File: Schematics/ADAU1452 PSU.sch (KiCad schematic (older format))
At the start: 74 parts, among them P301 CONN_2x1, P302 CONN_2x1, P303 PIN, P304 PIN, P305 PIN, P306 PIN, U301 IC-REG-XRP7659ISTR-F, U302 IC-REG-XRP7659ISTR-F, U303 XRP6272ITC5TR-F, U304 IC-REG-XC6210B332MR, U305 IC-REG-XC6210B332MR

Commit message: Schematic and PCB changes
Changed and corrected some footprints, removed capacitors, updated
documentation to change 1v5 SMPS to 1v2. Have not removed 1v2 LDO from
schematic yet.
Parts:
- removed C322, C323: 100u, OHDSP-Footprints-Pretty:SMD-0805, symbol CP1
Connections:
- wire segments 166 -> 162
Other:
- note added: "Add small diode\nfor quick discharge"
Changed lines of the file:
@@
-$EndComp
-$Comp
-L CP1 C322
-U 1 1 54D8DE5C
-P 7050 4150
-F 0 "C322" H 7100 4250 50  0000 L CNN
-F 1 "100u" H 7100 4050 50  0000 L CNN
-F 2 "OHDSP-Footprints-Pretty:SMD-0805" H 7050 4150 60  0000 C CNN
-F 3 "~" H 7050 4150 60  0000 C CNN
-	1    7050 4150
-	1    0    0    -1
 $EndComp
 $Comp
@@
 $EndComp
 $Comp
-L CP1 C323
-U 1 1 54D8E066
-P 7050 5300
-F 0 "C323" H 7100 5400 50  0000 L CNN
-F 1 "100u" H 7100 5200 50  0000 L CNN
-F 2 "OHDSP-Footprints-Pretty:SMD-0805" H 7050 5300 60  0000 C CNN
-F 3 "~" H 7050 5300 60  0000 C CNN
-	1    7050 5300
-	1    0    0    -1
-$EndComp
-$Comp
 L CP1 C341
 U 1 1 54D8E06F
@@
 L GNDD #PWR058
 U 1 1 54DA133C
-P 7050 4450
-F 0 "#PWR058" H 7050 4200 60  0001 C CNN
-F 1 "GNDD" H 7050 4300 60  0000 C CNN
-F 2 "" H 7050 4450 60  0000 C CNN
-F 3 "" H 7050 4450 60  0000 C CNN
-	1    7050 4450
+P 7400 4450
+F 0 "#PWR058" H 7400 4200 60  0001 C CNN
+F 1 "GNDD" H 7400 4300 60  0000 C CNN
+F 2 "" H 7400 4450 60  0000 C CNN
+F 3 "" H 7400 4450 60  0000 C CNN
+	1    7400 4450
 	1    0    0    -1
 $EndComp
@@
 L GNDD #PWR059
 U 1 1 54DA1370
-P 7050 5600
-F 0 "#PWR059" H 7050 5350 60  0001 C CNN
-F 1 "GNDD" H 7050 5450 60  0000 C CNN
-F 2 "" H 7050 5600 60  0000 C CNN
-F 3 "" H 7050 5600 60  0000 C CNN
-	1    7050 5600
+P 7400 5600
+F 0 "#PWR059" H 7400 5350 60  0001 C CNN
+F 1 "GNDD" H 7400 5450 60  0000 C CNN
+F 2 "" H 7400 5600 60  0000 C CNN
+F 3 "" H 7400 5600 60  0000 C CNN
+	1    7400 5600
 	1    0    0    -1
 $EndComp
@@
 	7400 3950 7400 3800
 Connection ~ 7700 3800
-Wire Wire Line
-	7050 3950 7050 3800
 Connection ~ 7400 3800
-Connection ~ 7050 3800
 Wire Wire Line
 	10650 3700 10650 3900
@@
 	7400 4950 7400 5100
 Connection ~ 7700 4950
-Wire Wire Line
-	7050 5100 7050 4950
 Connection ~ 7400 4950
-Connection ~ 7050 4950
 Wire Wire Line
 	10650 4900 10650 5050
@@
 	6150 4450 6150 4400
 Wire Wire Line
-	7050 4350 7050 4450
-Wire Wire Line
-	7050 5500 7050 5600
-Wire Wire Line
-	7050 4400 7700 4400
-Wire Wire Line
-	7400 4400 7400 4350
-Connection ~ 7050 4400
+	7400 4350 7400 4450
 Wire Wire Line
 	7700 4400 7700 4350
 Connection ~ 7400 4400
 Wire Wire Line
-	7050 5550 7700 5550
-Wire Wire Line
-	7400 5550 7400 5500
-Connection ~ 7050 5550
+	7400 5500 7400 5600
 Wire Wire Line
 	7700 5550 7700 5500
@@
 	1    0    0    -1
 $EndComp
+Text Notes 7700 1650 0    118  ~ 0
+Add small diode\nfor quick discharge
+Text Notes 7150 4900 0    79   ~ 0
+Add small diode\nfor quick discharge
+Text Notes 7350 3750 0    79   ~ 0
+Add small diode\nfor quick discharge
+Wire Wire Line
+	7400 4400 7700 4400
+Wire Wire Line
+	7700 5550 7400 5550
 $EndSCHEMATC

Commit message: Remove 1v2 LDO
Remove 1v2 LDO, not really needed...
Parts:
- removed C324, C332: 22u, OHDSP-Footprints-Pretty:SMD-0805, symbol C
- removed C327: 1u, OHDSP-Footprints-Pretty:SMD-0805, symbol C
- removed C336: 100n, OHDSP-Footprints-Pretty:SMD-0805, symbol C
- removed C339: 220u, OHDSP-Footprints-Pretty:CAP-TH-D6.3mmP2.5mm, symbol CP1
- removed R312: 100k, OHDSP-Footprints-Pretty:SMD-0805, symbol R
- removed R315: 34k8, OHDSP-Footprints-Pretty:SMD-0805, symbol R
- removed R316: 48k7, OHDSP-Footprints-Pretty:SMD-0805, symbol R
- removed U303: XRP6272ITC5TR-F, OHDSP-Footprints-Pretty:IC-TO-252-5L, symbol IC-REG-XRP6272
- C321: value 100n -> 1u
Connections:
- net labels removed: HT
- wire segments 162 -> 141
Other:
- moved on the sheet: C309, C313, C314, C316, C321, D303, L302, R301, R304, R305, U301

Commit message: R305 value change for 1v2
R305 value change for 1v2 from 1v5 value
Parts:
- R305: value 51k -> 97k6
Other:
- note added: "Can use 1% resistors for\nR305 and R304 although\n0.1% would be better."
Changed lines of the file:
@@
 P 5300 3100
 F 0 "R305" V 5380 3100 40  0000 C CNN
-F 1 "51k" V 5307 3101 40  0000 C CNN
+F 1 "97k6" V 5307 3101 40  0000 C CNN
 F 2 "OHDSP-Footprints-Pretty:SMD-0805" V 5230 3100 30  0001 C CNN
 F 3 "~" H 5300 3100 30  0000 C CNN
@@
 Wire Wire Line
 	1800 2050 1850 2050
+Text Notes 5450 3300 0    60   ~ 0
+Can use 1% resistors for\nR305 and R304 although\n0.1% would be better.
 $EndSCHEMATC

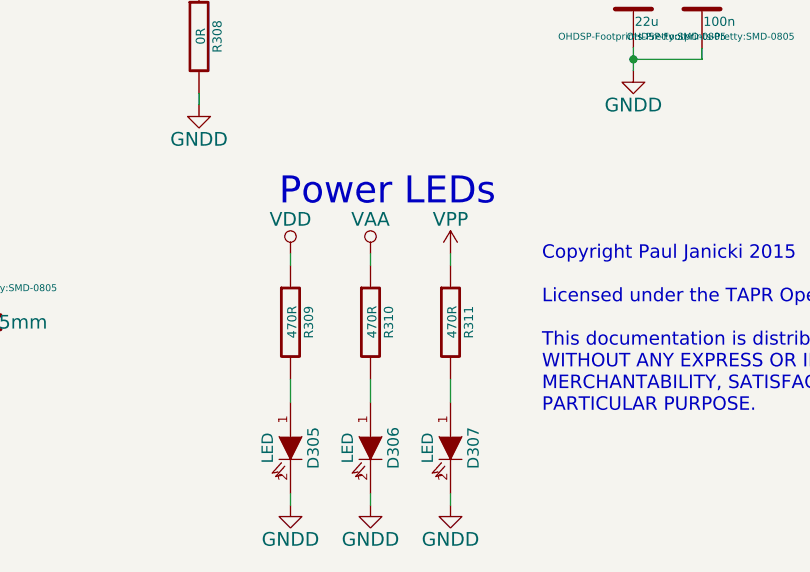
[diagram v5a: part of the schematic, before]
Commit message: PCB Work, minor schematic changes
Removed cap and LED, changed one net label
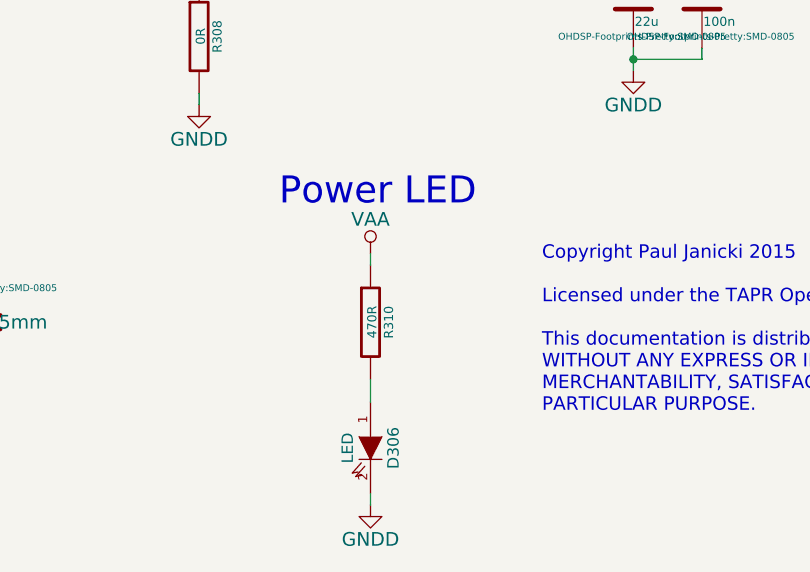
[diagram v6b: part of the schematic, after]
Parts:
- removed D305, D307: LED, OHDSP-Footprints-Pretty:SMD-1206, symbol LED
- removed R309, R311: 470R, OHDSP-Footprints-Pretty:SMD-0805, symbol R
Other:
- note added: "Power LED"
- note removed: "Power LEDs"
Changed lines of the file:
@@
 Two sets of screw terminals\nOne for 5V-16V self power\nOne set for 5V - will power the Pi as well\nDo not put 16V up the Pi!
-$Comp
-L LED D305
-U 1 1 54E58EE4
-P 5900 7250
-F 0 "D305" H 5900 7350 50  0000 C CNN
-F 1 "LED" H 5900 7150 50  0000 C CNN
-F 2 "OHDSP-Footprints-Pretty:SMD-1206" H 5900 7250 60  0001 C CNN
-F 3 "" H 5900 7250 60  0000 C CNN
-	1    5900 7250
-	0    1    1    0
-$EndComp
-$Comp
-L R R309
-U 1 1 54E59038
-P 5900 6700
-F 0 "R309" V 5980 6700 40  0000 C CNN
-F 1 "470R" V 5907 6701 40  0000 C CNN
-F 2 "OHDSP-Footprints-Pretty:SMD-0805" V 5830 6700 30  0001 C CNN
-F 3 "~" H 5900 6700 30  0000 C CNN
-	1    5900 6700
-	1    0    0    -1
-$EndComp
-Wire Wire Line
-	5900 6950 5900 7050
-$Comp
-L GNDD #PWR078
-U 1 1 54E59324
-P 5900 7500
-F 0 "#PWR078" H 5900 7250 60  0001 C CNN
-F 1 "GNDD" H 5900 7350 60  0000 C CNN
-F 2 "" H 5900 7500 60  0000 C CNN
-F 3 "" H 5900 7500 60  0000 C CNN
-	1    5900 7500
-	1    0    0    -1
-$EndComp
-Wire Wire Line
-	5900 7500 5900 7450
 $Comp
 L LED D306
@@
 	6250 6950 6250 7050
 $Comp
-L GNDD #PWR079
+L GNDD #PWR078
 U 1 1 54E5949B
 P 6250 7500
-F 0 "#PWR079" H 6250 7250 60  0001 C CNN
+F 0 "#PWR078" H 6250 7250 60  0001 C CNN
 F 1 "GNDD" H 6250 7350 60  0000 C CNN
 F 2 "" H 6250 7500 60  0000 C CNN
@@
 	6250 7500 6250 7450
 $Comp
-L LED D307
-U 1 1 54E5950E
-P 6600 7250
-F 0 "D307" H 6600 7350 50  0000 C CNN
-F 1 "LED" H 6600 7150 50  0000 C CNN
-F 2 "OHDSP-Footprints-Pretty:SMD-1206" H 6600 7250 60  0001 C CNN
-F 3 "" H 6600 7250 60  0000 C CNN
-	1    6600 7250
-	0    1    1    0
-$EndComp
-$Comp
-L R R311
-U 1 1 54E59514
-P 6600 6700
-F 0 "R311" V 6680 6700 40  0000 C CNN
-F 1 "470R" V 6607 6701 40  0000 C CNN
-F 2 "OHDSP-Footprints-Pretty:SMD-0805" V 6530 6700 30  0001 C CNN
-F 3 "~" H 6600 6700 30  0000 C CNN
-	1    6600 6700
-	1    0    0    -1
-$EndComp
-Wire Wire Line
-	6600 6950 6600 7050
-$Comp
-L GNDD #PWR080
-U 1 1 54E5951B
-P 6600 7500
-F 0 "#PWR080" H 6600 7250 60  0001 C CNN
-F 1 "GNDD" H 6600 7350 60  0000 C CNN
-F 2 "" H 6600 7500 60  0000 C CNN
-F 3 "" H 6600 7500 60  0000 C CNN
-	1    6600 7500
-	1    0    0    -1
-$EndComp
-Wire Wire Line
-	6600 7500 6600 7450
-$Comp
-L VAA #PWR081
+L VAA #PWR079
 U 1 1 54E59D5A
 P 6250 6400
-F 0 "#PWR081" H 6250 6250 60  0001 C CNN
+F 0 "#PWR079" H 6250 6250 60  0001 C CNN
 F 1 "VAA" H 6250 6550 60  0000 C CNN
 F 2 "" H 6250 6400 60  0000 C CNN
@@
 	1    0    0    -1
 $EndComp
-$Comp
-L VPP #PWR082
-U 1 1 54E59DAF
-P 6600 6400
-F 0 "#PWR082" H 6600 6250 60  0001 C CNN
-F 1 "VPP" H 6600 6550 60  0000 C CNN
-F 2 "" H 6600 6400 60  0000 C CNN
-F 3 "" H 6600 6400 60  0000 C CNN
-	1    6600 6400
-	1    0    0    -1
-$EndComp
-Wire Wire Line
-	6600 6400 6600 6450
 Wire Wire Line
 	6250 6400 6250 6450
-Wire Wire Line
-	5900 6400 5900 6450
 Text Notes 5850 6200 0    118  ~ 0
-Power LEDs
+Power LED
 $Comp
 L DIODE D301
@@
 $EndComp
 $Comp
-L GNDD #PWR083
+L GNDD #PWR080
 U 1 1 54E676A2
 P 850 7350
-F 0 "#PWR083" H 850 7100 60  0001 C CNN
+F 0 "#PWR080" H 850 7100 60  0001 C CNN
 F 1 "GNDD" H 850 7200 60  0000 C CNN
 F 2 "" H 850 7350 60  0000 C CNN
@@
 $EndComp
 $Comp
-L GNDD #PWR084
+L GNDD #PWR081
 U 1 1 54E6778E
 P 1050 7350
-F 0 "#PWR084" H 1050 7100 60  0001 C CNN
+F 0 "#PWR081" H 1050 7100 60  0001 C CNN
 F 1 "GNDD" H 1050 7200 60  0000 C CNN
 F 2 "" H 1050 7350 60  0000 C CNN
@@
 $EndComp
 $Comp
-L GNDD #PWR085
+L GNDD #PWR082
 U 1 1 54E677E4
 P 1250 7350
-F 0 "#PWR085" H 1250 7100 60  0001 C CNN
+F 0 "#PWR082" H 1250 7100 60  0001 C CNN
 F 1 "GNDD" H 1250 7200 60  0000 C CNN
 F 2 "" H 1250 7350 60  0000 C CNN
@@
 $EndComp
 $Comp
-L GNDD #PWR086
+L GNDD #PWR083
 U 1 1 54E6783A
 P 1450 7350
-F 0 "#PWR086" H 1450 7100 60  0001 C CNN
+F 0 "#PWR083" H 1450 7100 60  0001 C CNN
 F 1 "GNDD" H 1450 7200 60  0000 C CNN
 F 2 "" H 1450 7350 60  0000 C CNN
@@
 	6400 1950 6400 2050
 Connection ~ 6400 2050
-$Comp
-L VDD #PWR087
-U 1 1 54EE7A05
-P 5900 6400
-F 0 "#PWR087" H 5900 6250 60  0001 C CNN
-F 1 "VDD" H 5900 6550 60  0000 C CNN
-F 2 "" H 5900 6400 60  0000 C CNN
-F 3 "" H 5900 6400 60  0000 C CNN
-	1    5900 6400
-	1    0    0    -1
-$EndComp
 Wire Wire Line
 	5850 2700 6550 2700
 $Comp
-L GNDD #PWR088
+L GNDD #PWR084
 U 1 1 54EE87C5
 P 2450 2550
-F 0 "#PWR088" H 2450 2300 60  0001 C CNN
+F 0 "#PWR084" H 2450 2300 60  0001 C CNN
 F 1 "GNDD" H 2450 2400 60  0000 C CNN
 F 2 "" H 2450 2550 60  0000 C CNN

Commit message: PCB work, Running Electrical Rule Check
PCB work, Running Electrical Rule Check:
Added no connects to schematics, added missing pull up on EEPROM, remove
USB_CLK/USB_RESET label on USB/I2C header and added NC. Minor change on
Pi connectors.
Removed old large PCB file.
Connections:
- net VCOM: now also C315.1, C317.1, C319.1, C325.1, C326.1, C328.1, C329.1, L303.2, R306.1, R313.1, R314.1, U304.1 (VIN), U305.1 (VIN)
- no-connect marks 0 -> 2
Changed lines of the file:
@@
 L VCOM #PWR071
 U 1 1 54E9EE9E
-P 6850 3800
-F 0 "#PWR071" H 6850 3650 60  0001 C CNN
-F 1 "VCOM" H 6850 3950 60  0000 C CNN
-F 2 "" H 6850 3800 60  0000 C CNN
-F 3 "" H 6850 3800 60  0000 C CNN
-	1    6850 3800
+P 6850 3750
+F 0 "#PWR071" H 6850 3600 60  0001 C CNN
+F 1 "VCOM" H 6850 3900 60  0000 C CNN
+F 2 "" H 6850 3750 60  0000 C CNN
+F 3 "" H 6850 3750 60  0000 C CNN
+	1    6850 3750
 	1    0    0    -1
 $EndComp
@@
 Text Notes 5450 3300 0    60   ~ 0
 Can use 1% resistors for\nR305 and R304 although\n0.1% would be better.
+NoConn ~ 8550 4200
+NoConn ~ 8550 5350
+Connection ~ 10300 3800
+Connection ~ 7150 3800
+Wire Wire Line
+	6850 3750 6850 3800
+Connection ~ 6850 3800
+Connection ~ 10300 4950
+Connection ~ 1400 1850
+$Comp
+L PWR_FLAG #FLG085
+U 1 1 55004FD5
+P 3500 2800
+F 0 "#FLG085" H 3500 2895 30  0001 C CNN
+F 1 "PWR_FLAG" H 3500 2980 30  0000 C CNN
+F 2 "" H 3500 2800 60  0000 C CNN
+F 3 "" H 3500 2800 60  0000 C CNN
+	1    3500 2800
+	1    0    0    -1
+$EndComp
+$Comp
+L GNDD #PWR086
+U 1 1 55005056
+P 3500 2850
+F 0 "#PWR086" H 3500 2600 60  0001 C CNN
+F 1 "GNDD" H 3500 2700 60  0000 C CNN
+F 2 "" H 3500 2850 60  0000 C CNN
+F 3 "" H 3500 2850 60  0000 C CNN
+	1    3500 2850
+	1    0    0    -1
+$EndComp
+Wire Wire Line
+	3500 2850 3500 2800
 $EndSCHEMATC
